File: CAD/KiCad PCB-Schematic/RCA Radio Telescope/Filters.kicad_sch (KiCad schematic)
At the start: 9 parts, among them U10 MIC5365-1.8YC5-TR, U11 MIC5365-3.3YC5-TR, U3 SKY13588-460LF, U8 SKY13588-460LF, U9 SN74AVC2T244DQER

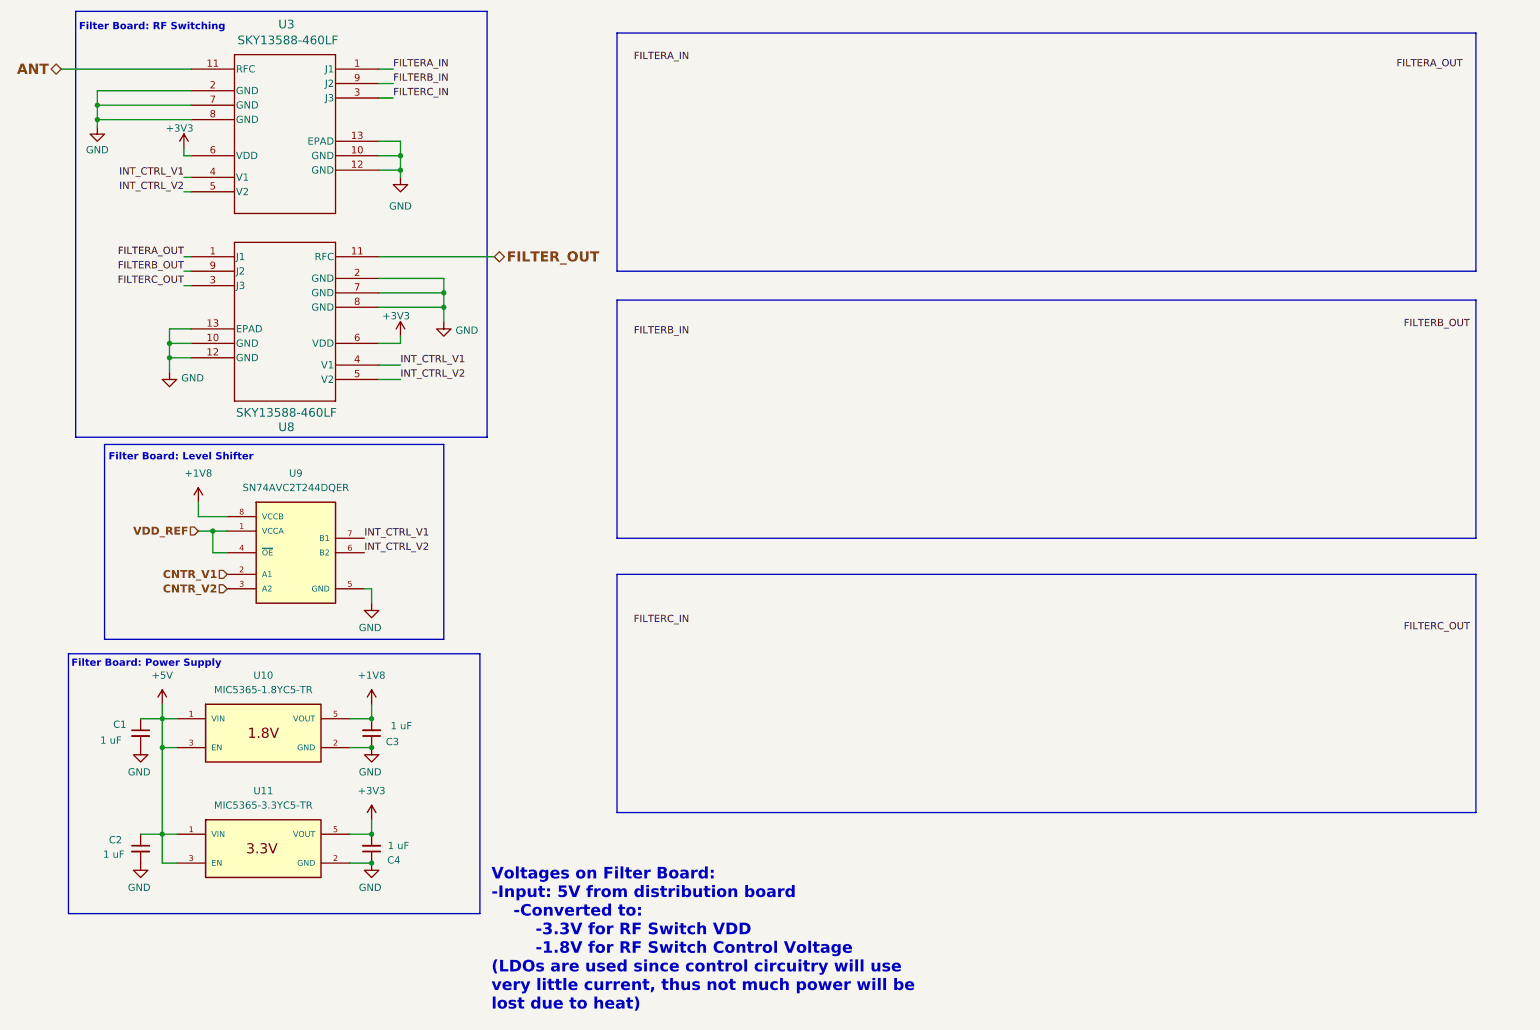
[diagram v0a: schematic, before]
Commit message: Updated Schematic
Updated Root Schematic to v1.4
- Added Screw Terminals for 5V In/Out, 3V Out for LNA
- Reorganized Skylark Shed Power to include Battery, Inverter, and AC-DC Adapter
- Added TODO list

Updated PowerDataDistribute Schematic to v1.1
- Removed labels for USB signals and replaced it with single USB_OUT signal
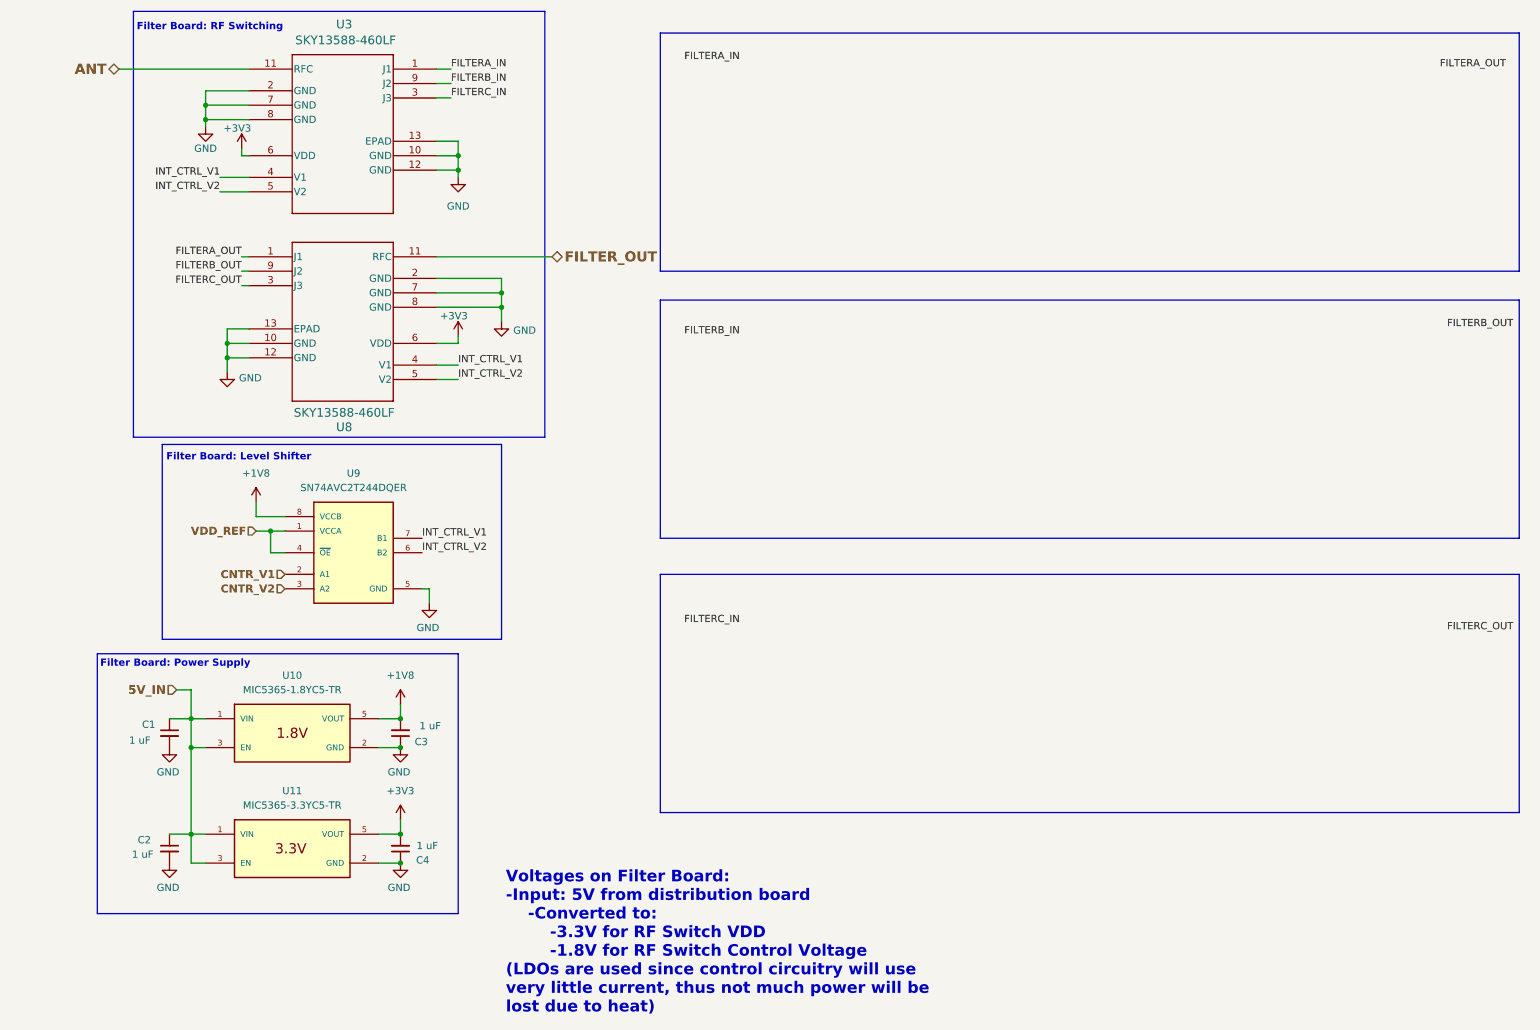
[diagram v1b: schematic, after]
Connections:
- net +5V renamed 5V_IN
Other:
- moved on the sheet: C1, C2, C3, C4, U10, U11, U3, U8, U9

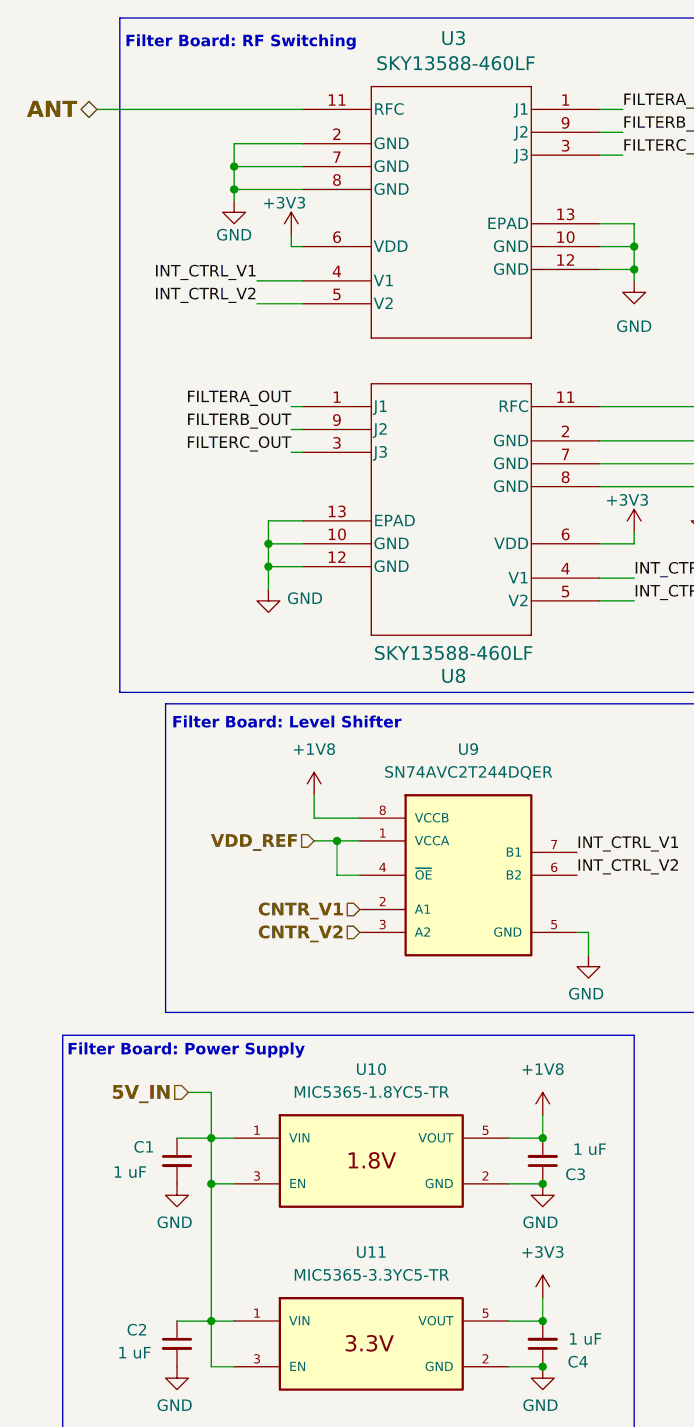
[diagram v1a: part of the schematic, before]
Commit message: Updated Schematic
Updated Root Schematic to v1.5, Filters to v1.1, and PowerDataDistribute to v1.1.
- Updated part references to be more consistent
- Added missing GND label for SDR GPO
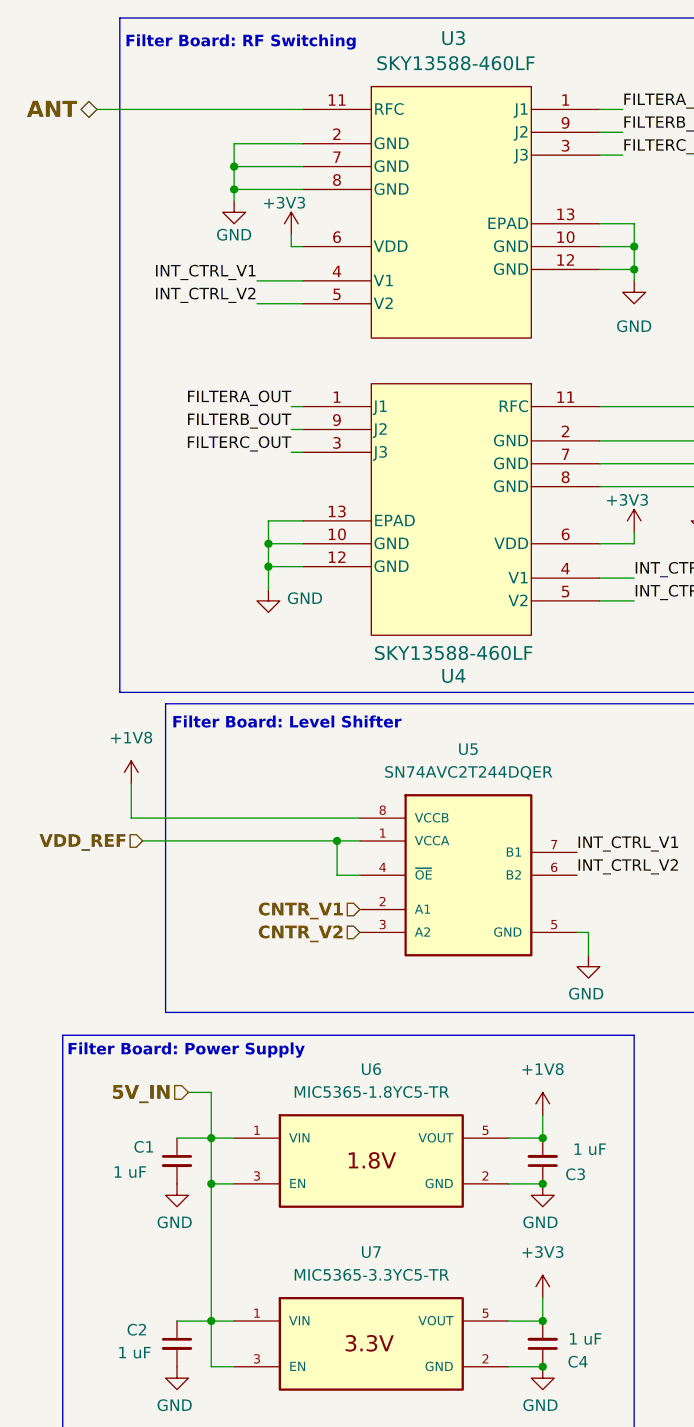
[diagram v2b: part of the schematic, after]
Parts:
- renumbered U8 to U4, U9 to U5, U10 to U6, U11 to U7
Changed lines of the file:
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@@
 		(title "Filter Section")
 		(date "2025-02-27")
-		(rev "Version 1.0")
+		(rev "Version 1.1")
 	)
 	(junction
@@
 	(wire
 		(pts
-			(xy 57.15 107.95) (xy 59.69 107.95)
+			(xy 38.1 107.95) (xy 59.69 107.95)
 		)
 		(stroke
@@
 	(wire
 		(pts
-			(xy 62.23 105.41) (xy 57.15 105.41)
+			(xy 62.23 105.41) (xy 36.83 105.41)
 		)
 		(stroke
@@
 	(wire
 		(pts
-			(xy 57.15 102.87) (xy 57.15 105.41)
+			(xy 36.83 101.6) (xy 36.83 105.41)
 		)
 		(stroke
@@
 	(hierarchical_label "VDD_REF"
 		(shape input)
-		(at 57.15 107.95 180)
+		(at 38.1 107.95 180)
 		(effects
 			(font
@@
 	(symbol
 		(lib_id "power:+1V8")
-		(at 57.15 102.87 0)
+		(at 36.83 101.6 0)
 		(unit 1)
 		(exclude_from_sim no)
@@
 		(fields_autoplaced yes)
 		(property "Reference" "#PWR024"
-			(at 57.15 106.68 0)
+			(at 36.83 105.41 0)
 			(effects
 				(font
@@
 		)
 		(property "Value" "+1V8"
-			(at 57.15 97.79 0)
+			(at 36.83 96.52 0)
 			(effects
 				(font
@@
 		)
 		(property "Footprint" ""
-			(at 57.15 102.87 0)
+			(at 36.83 101.6 0)
 			(effects
 				(font
@@
 		)
 		(property "Datasheet" ""
-			(at 57.15 102.87 0)
+			(at 36.83 101.6 0)
 			(effects
 				(font
@@
 		)
 		(property "Description" "Power symbol creates a global label with name \"+1V8\""
-			(at 57.15 102.87 0)
+			(at 36.83 101.6 0)
 			(effects
 				(font
@@
 		(dnp no)
 		(fields_autoplaced yes)
-		(property "Reference" "U11"
+		(property "Reference" "U7"
 			(at 63.5 153.67 0)
 			(effects
@@
 			(project ""
 				(path "/1630c5ee-b70a-455e-85ba-86a73955b8fd/017a3eae-b6d3-453d-be97-44a0879a04d4"
-					(reference "U11")
+					(reference "U7")
 					(unit 1)
 				)
@@
 		(on_board yes)
 		(dnp no)
-		(property "Reference" "U8"
+		(property "Reference" "U4"
 			(at 72.644 89.662 0)
 			(effects
@@
 			(project ""
 				(path "/1630c5ee-b70a-455e-85ba-86a73955b8fd/017a3eae-b6d3-453d-be97-44a0879a04d4"
-					(reference "U8")
+					(reference "U4")
 					(unit 1)
 				)
@@
 		(dnp no)
 		(fields_autoplaced yes)
-		(property "Reference" "U9"
+		(property "Reference" "U5"
 			(at 74.295 97.79 0)
 			(effects
@@
 			(project ""
 				(path "/1630c5ee-b70a-455e-85ba-86a73955b8fd/017a3eae-b6d3-453d-be97-44a0879a04d4"
-					(reference "U9")
+					(reference "U5")
 					(unit 1)
 				)
@@
 		(dnp no)
 		(fields_autoplaced yes)
-		(property "Reference" "U10"
+		(property "Reference" "U6"
 			(at 63.5 133.35 0)
 			(effects
@@
 			(project ""
 				(path "/1630c5ee-b70a-455e-85ba-86a73955b8fd/017a3eae-b6d3-453d-be97-44a0879a04d4"
-					(reference "U10")
+					(reference "U6")
 					(unit 1)
 				)

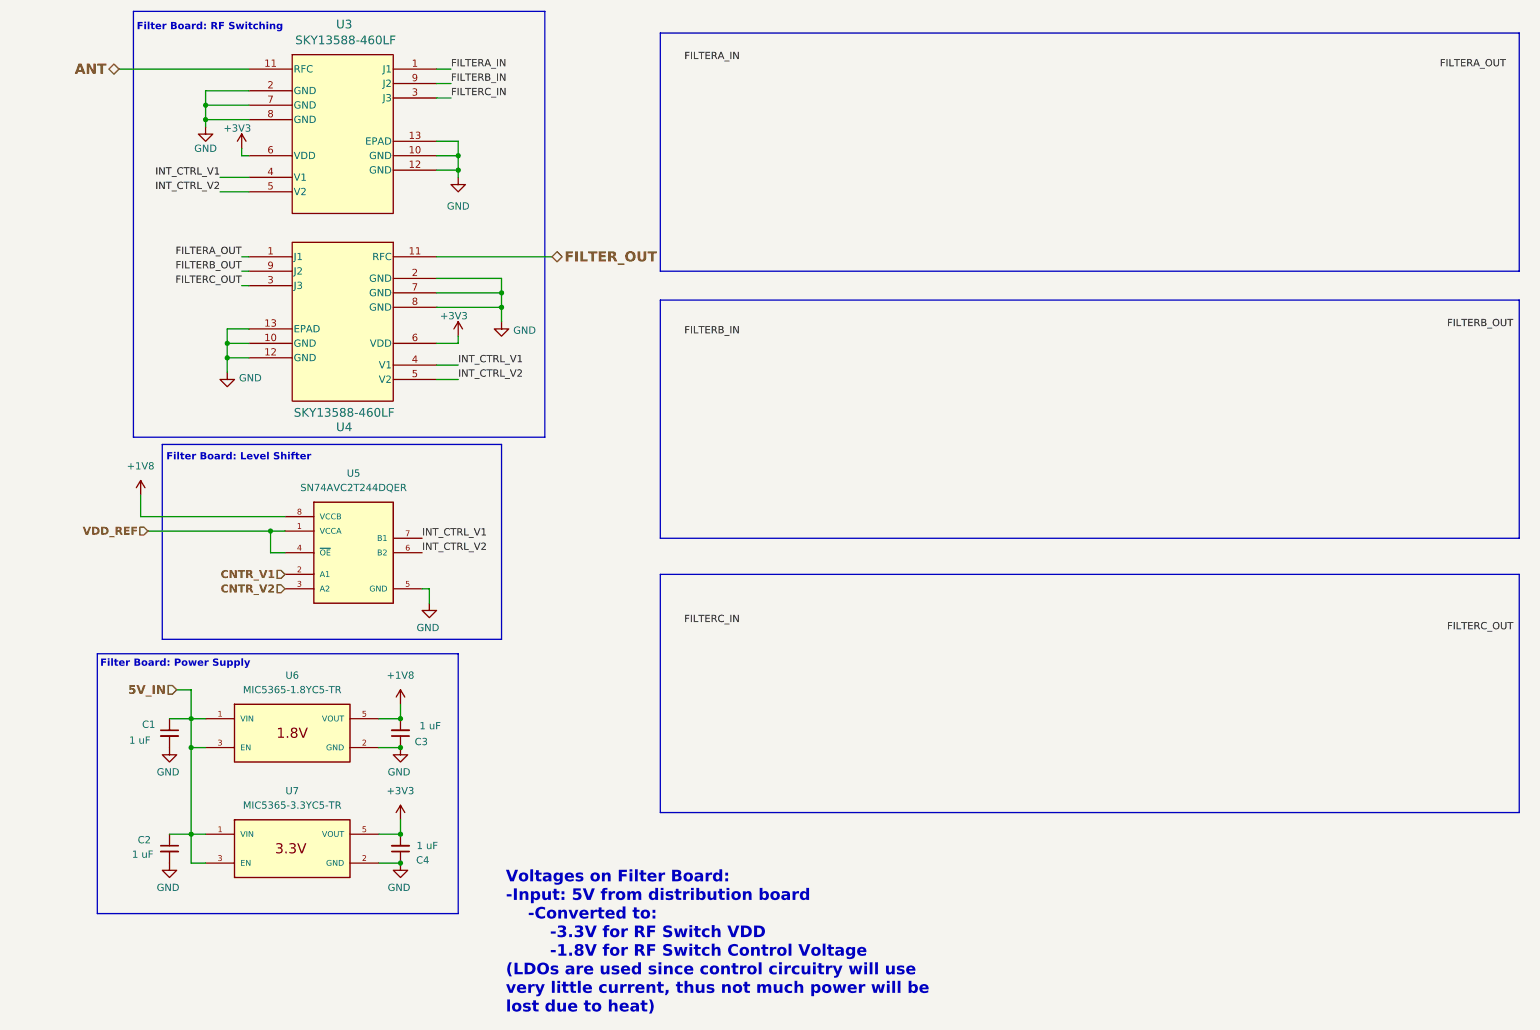
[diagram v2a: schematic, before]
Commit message: Updated Filter Schematic to v1.2
- Fixed switch logic to better suit the footprint layout (Swapped J1 and J2 on one switch (secondary one) and swapped the v1 and v2 pins on the same switch)
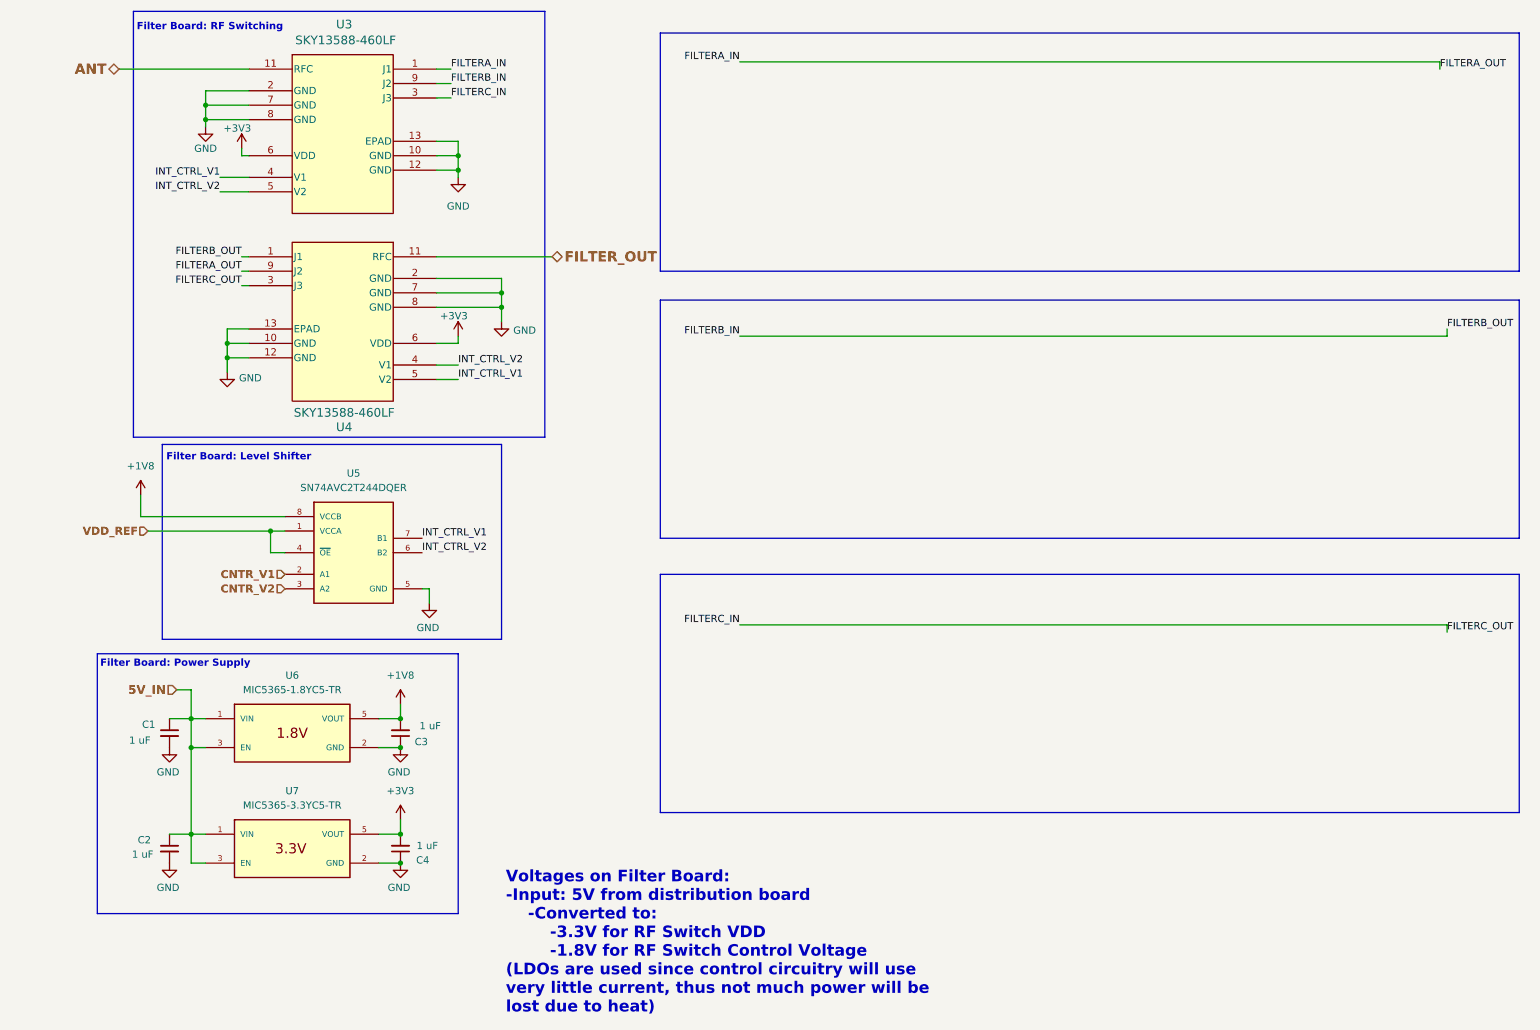
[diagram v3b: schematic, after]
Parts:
- U3, U4: footprint QFN12_SKY -> Library:QFN12_SKY
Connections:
- net FILTERA_OUT is gone; now on net FILTERB_IN: U4.1 (J1)
- net FILTERB_OUT is gone; now on net FILTERA_IN: U4.9 (J2)
- net FILTERC_OUT is gone; now on net FILTERC_IN: U4.3 (J3)
- net INT_CTRL_V1: now also U4.5 (V2); no longer U4.4 (V1)
- net INT_CTRL_V2: now also U4.4 (V1); no longer U4.5 (V2)
